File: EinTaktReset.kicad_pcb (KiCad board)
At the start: 2 copper layers, 58 parts, among them IC1 74LS624, J1 3PinTerminalBlocktg, J2 3PinTerminalBlocktg, J3 2PinTerminalBlocktg, J4 3PinTerminalBlocktg, J5 2PinTerminalBlocktg, P1 CONN_02X10, P4 CONN_02X10, SW1 SWITCH_INV, SW10 SPST, SW11 SPST, SW12 SPST, SW13 SPST, SW2 SWITCH_INV, SW3 SPST, SW4 SPST, SW5 SPST, SW6 SWITCH_INV, SW7 SPST, SW8 SPST, SW9 SPST, U1 74LS132, U2 74540En, U3 74HCT541_PWR, U4 74LS32, U5 74LS00

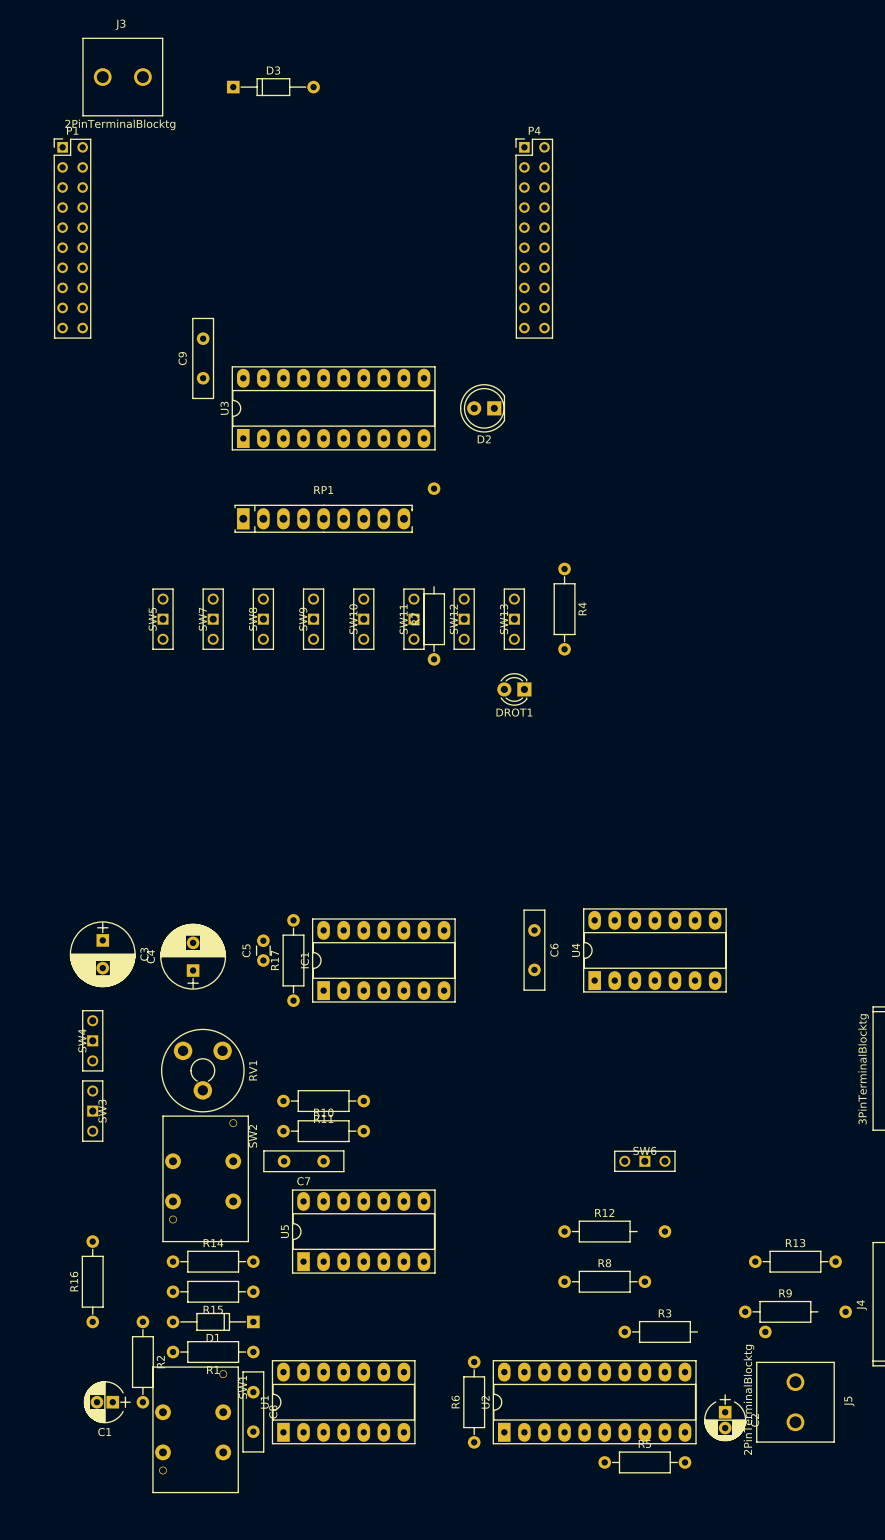
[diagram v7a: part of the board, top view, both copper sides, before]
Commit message: mit libraryproblemen gedealt (teilweise erfolgreich), kabellegen angefangen
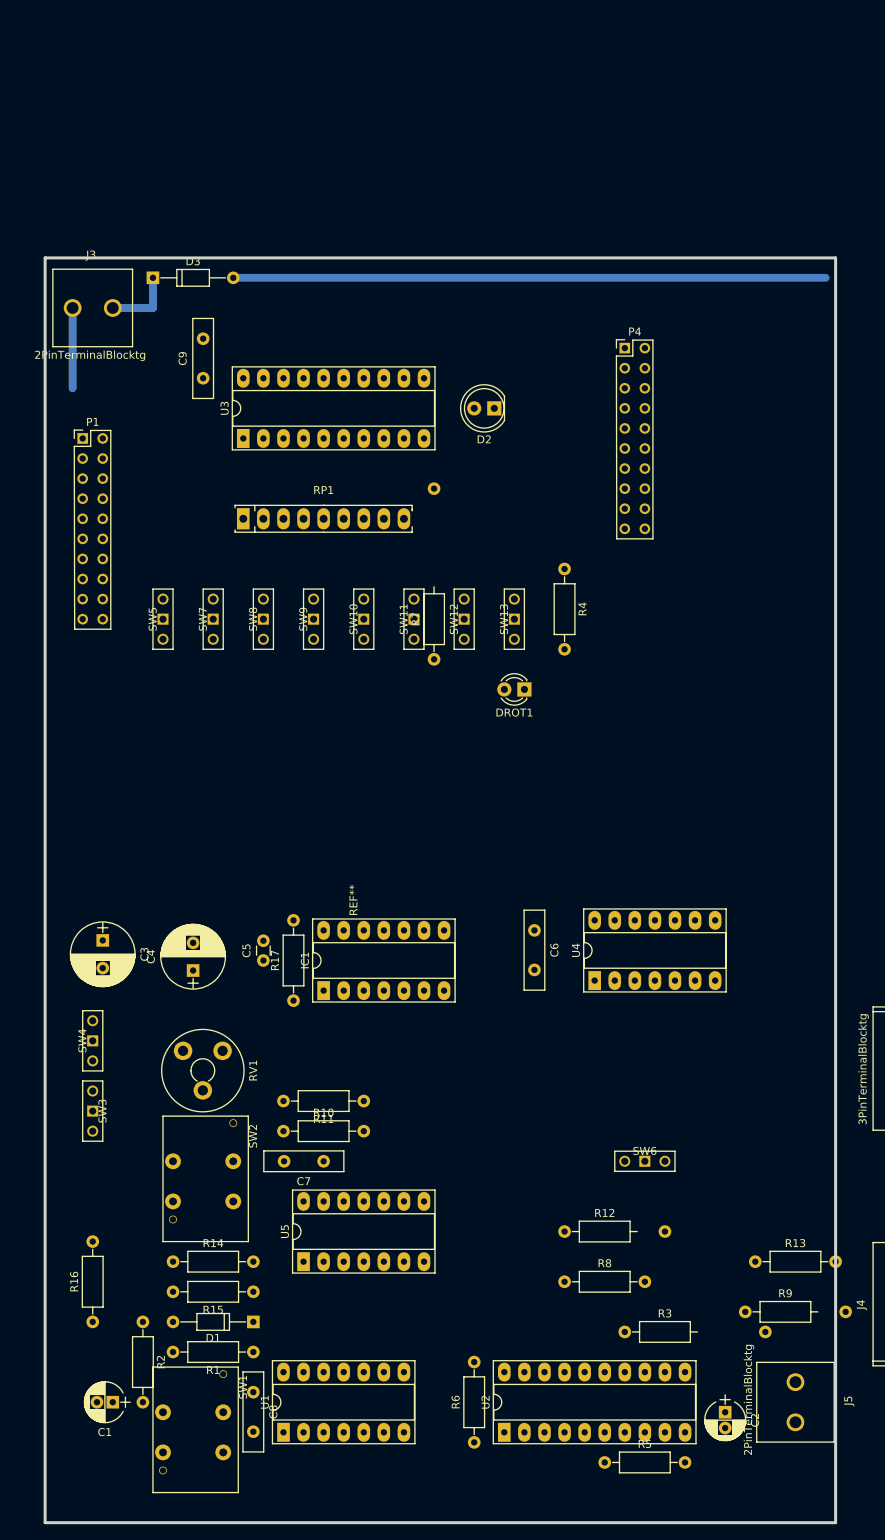
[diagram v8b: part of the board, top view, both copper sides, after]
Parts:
- added REF**: EuroBoard160mmX100mm, EuroBoard_Outline:EuroBoard160mmX100mm, F.Cu at (109.2, 200.7)
- moved P1 36.9 mm to (14.0, 63.5)
- moved J3 29.5 mm to (15.2, 47.0)
- moved P4 28.4 mm to (82.5, 52.1)
- moved D3 26.2 mm to (22.9, 43.2)
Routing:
- net GND: track 0.00 -> 85.1 mm
- net VCC: track 0.00 -> 8.89 mm
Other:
- board outline added: 100 x 160 mm
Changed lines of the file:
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@@
-(kicad_pcb (version 20171130) (host pcbnew 5.0.0-rc2-dev-unknown-5a90858~64~ubuntu16.04.1)
+(kicad_pcb (version 20171130) (host pcbnew no-vcs-found-bf44d39~61~ubuntu16.04.1)
   (general
     (thickness 1.6)
     (drawings 0)
-    (tracks 0)
+    (tracks 4)
     (zones 0)
-    (modules 58)
+    (modules 59)
     (nets 63)
   )
@@
   )
   (module 2PinTerminalBlocktg (layer F.Cu)
-    (at 19.05 17.78)
+    (at 15.24 46.99)
     (descr "<b>WR-TBL Serie 2165 - 5.08mm Horizontal Entry Modular with Rising Cage Clamp - 3.5mm2 Wires, 2 Pins")
     (fp_text reference J3 (at -0.196539 -6.71131) (layer F.SilkS)
@@
   )
   (module Diodes_ThroughHole:D_DO-35_SOD27_P10.16mm_Horizontal (layer F.Cu)
-    (at 33.02 19.05)
+    (at 22.86 43.18)
     (descr "D, DO-35_SOD27 series, Axial, Horizontal, pin pitch=10.16mm, , length*diameter=4*2mm^2, , http://www.diodes.com/_files/packages/DO-35.pdf")
     (tags "D DO-35_SOD27 series Axial Horizontal pin pitch 10.16mm  length 4mm diameter 2mm")
@@
   )
   (module tg_foodprint:Pin_Header_Straight_2x10_Pitch2.00mmBonsai.pretty (layer F.Cu)
-    (at 11.43 26.67)
+    (at 13.97 63.5)
     (descr "Through hole straight pin header, 2x10, 2.00mm pitch, double rows")
     (tags "Through hole pin header THT 2x10 2.00mm double row")
@@
   )
   (module tg_foodprint:Pin_Header_Straight_2x10_Pitch2.00mmBonsai.pretty (layer F.Cu)
-    (at 69.85 26.67)
+    (at 82.55 52.07)
     (descr "Through hole straight pin header, 2x10, 2.00mm pitch, double rows")
     (tags "Through hole pin header THT 2x10 2.00mm double row")
@@
     )
   )
+  (module EuroBoard_Outline:EuroBoard160mmX100mm (layer F.Cu)
+    (at 109.22 200.66 90)
+    (descr "Outline, Eurocard, 100x160mm,")
+    (tags "Outline, Eurocard, 100x160mm,")
+    (fp_text reference REF** (at 78.74 -60.96 90) (layer F.SilkS)
+      (effects (font (size 1 1) (thickness 0.15)))
+    )
+    (fp_text value EuroBoard160mmX100mm (at 85.09 -35.56 90) (layer F.Fab)
+      (effects (font (size 1 1) (thickness 0.15)))
+    )
+    (fp_line (start 0 -100) (end 0 0) (layer Edge.Cuts) (width 0.38))
+    (fp_line (start 0 0) (end 160 0) (layer Edge.Cuts) (width 0.38))
+    (fp_line (start 160 0) (end 160 -100) (layer Edge.Cuts) (width 0.38))
+    (fp_line (start 160 -100) (end 0 -100) (layer Edge.Cuts) (width 0.38))
+  )
+  (segment (start 33.02 43.18) (end 107.95 43.18) (width 1) (layer B.Cu) (net 12) (status 400000))
+  (segment (start 12.7 46.99) (end 12.7 57.15) (width 1) (layer B.Cu) (net 12) (status 400000))
+  (segment (start 22.86 43.18) (end 22.86 46.99) (width 1) (layer B.Cu) (net 13) (status 400000))
+  (segment (start 22.86 46.99) (end 17.78 46.99) (width 1) (layer B.Cu) (net 13) (status 800000))
 )
